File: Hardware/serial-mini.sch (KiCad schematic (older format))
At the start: 70 parts, among them J1 PICKIT V3 Header, J2 USB Micro B, J3 Serial Port, Q1 IRLML2060, Q2 IRLML2060, Q3 IRLML2060, U1 SIT2001BI-S2-33S-100.000000D, U2 FT230XQ-R, U3 DSPIC33CK64MP102, U4 SN74AHC14RGYR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

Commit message: Continue routing
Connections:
- net Status: now reaches U3.RB12
- net Status: now also D5.1, TP6.1
- removed net 2V@15mA: D5.1, TP6.1, U3.RA1
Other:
- moved on the sheet: D5, R17, TP6
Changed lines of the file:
@@
 	12600 6800 12600 6500
 Connection ~ 12600 6800
-NoConn ~ 9000 4750
 NoConn ~ 3100 4300
 NoConn ~ 3100 4000
@@
 L power:+5V #PWR015
 U 1 1 5F297A7B
-P 4550 3750
-F 0 "#PWR015" H 4550 3600 50  0001 C CNN
-F 1 "+5V" H 4565 3923 50  0000 C CNN
-F 2 "" H 4550 3750 50  0001 C CNN
-F 3 "" H 4550 3750 50  0001 C CNN
-	1    4550 3750
+P 4050 3700
+F 0 "#PWR015" H 4050 3550 50  0001 C CNN
+F 1 "+5V" H 4065 3873 50  0000 C CNN
+F 2 "" H 4050 3700 50  0001 C CNN
+F 3 "" H 4050 3700 50  0001 C CNN
+	1    4050 3700
 	0    -1   -1   0
 $EndComp
@@
 L serial-mini:VAOL-S8WR4 D5
 U 1 1 5F2EDA7B
-P 5400 3750
-F 0 "D5" H 5600 4138 60  0000 C CNN
-F 1 "VAOL-S8WR4" H 5600 4032 60  0000 C CNN
-F 2 "footprints:VAOL-S8WR4" H 5600 3390 60  0001 C CNN
-F 3 "http://vcclite.com/_pdf/VAOL-S8WR4-LED-0805-white.pdf" H 5600 4032 60  0001 C CNN
-	1    5400 3750
+P 4900 3700
+F 0 "D5" H 5100 4088 60  0000 C CNN
+F 1 "VAOL-S8WR4" H 5100 3982 60  0000 C CNN
+F 2 "footprints:VAOL-S8WR4" H 5100 3340 60  0001 C CNN
+F 3 "http://vcclite.com/_pdf/VAOL-S8WR4-LED-0805-white.pdf" H 5100 3982 60  0001 C CNN
+	1    4900 3700
 	1    0    0    -1
 $EndComp
@@
 $EndComp
 Wire Wire Line
-	5800 3750 5850 3750
+	5300 3700 5350 3700
 $Comp
 L serial-mini-rescue:RESISTOR0603-serial-mini-serial-mini R17
 U 1 1 5F3D4344
-P 5050 3750
-F 0 "R17" H 5050 4050 45  0000 C CNN
-F 1 "133" H 5050 3966 45  0000 C CNN
-F 2 "Resistor_SMD:R_0603_1608Metric_Pad1.05x0.95mm_HandSolder" H 5050 3900 20  0001 C CNN
-F 3 "" H 5050 3750 60  0001 C CNN
-F 4 " " H 5050 3871 60  0000 C CNN "Field4"
-	1    5050 3750
-	1    0    0    -1
-$EndComp
-Wire Wire Line
-	5250 3750 5400 3750
-Wire Wire Line
-	4850 3750 4550 3750
+P 4550 3700
+F 0 "R17" H 4550 4000 45  0000 C CNN
+F 1 "133" H 4550 3916 45  0000 C CNN
+F 2 "Resistor_SMD:R_0603_1608Metric_Pad1.05x0.95mm_HandSolder" H 4550 3850 20  0001 C CNN
+F 3 "" H 4550 3700 60  0001 C CNN
+F 4 " " H 4550 3821 60  0000 C CNN "Field4"
+	1    4550 3700
+	1    0    0    -1
+$EndComp
+Wire Wire Line
+	4750 3700 4900 3700
+Wire Wire Line
+	4350 3700 4050 3700
 Wire Wire Line
 	10050 6500 10100 6500
@@
 Text Label 10800 6500 0    50   ~ 0
 3V@20mA
-Text Label 5850 3750 0    50   ~ 0
+Text Label 5350 3700 0    50   ~ 0
 2V@15mA
 $Comp
@@
 L Connector:TestPoint TP6
 U 1 1 5F68536D
-P 5850 3750
-F 0 "TP6" H 5792 3776 50  0000 R CNN
-F 1 "TestPoint" H 5792 3867 50  0000 R CNN
-F 2 "TestPoint:TestPoint_Pad_1.0x1.0mm" H 6050 3750 50  0001 C CNN
-F 3 "~" H 6050 3750 50  0001 C CNN
-	1    5850 3750
-	-1   0    0    1
-$EndComp
-Connection ~ 5850 3750
-Wire Wire Line
-	5850 3750 6200 3750
+P 5350 3700
+F 0 "TP6" H 5292 3726 50  0000 R CNN
+F 1 "TestPoint" H 5292 3817 50  0000 R CNN
+F 2 "TestPoint:TestPoint_Pad_1.0x1.0mm" H 5550 3700 50  0001 C CNN
+F 3 "~" H 5550 3700 50  0001 C CNN
+	1    5350 3700
+	-1   0    0    1
+$EndComp
 $Comp
 L Connector:TestPoint TP1
@@
 NoConn ~ 4050 4700
 NoConn ~ 7550 3200
+Text GLabel 9000 4750 2    50   Input ~ 0
+Status
+Text GLabel 5350 3700 2    50   Input ~ 0
+Status
+NoConn ~ 6200 3750
 $EndSCHEMATC

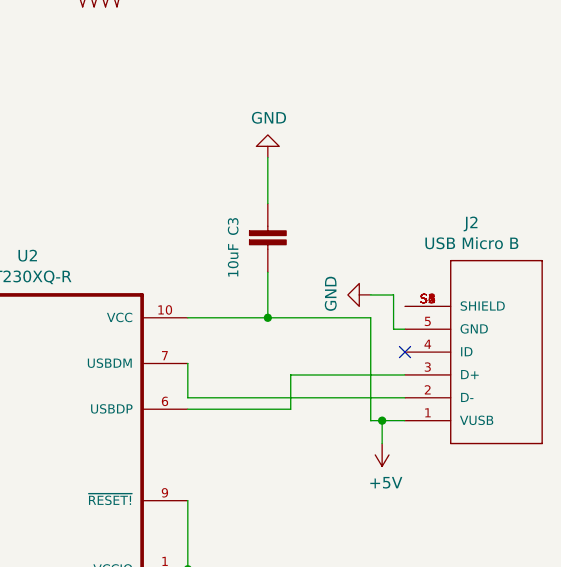
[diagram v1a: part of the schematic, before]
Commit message: Add missing courtyards
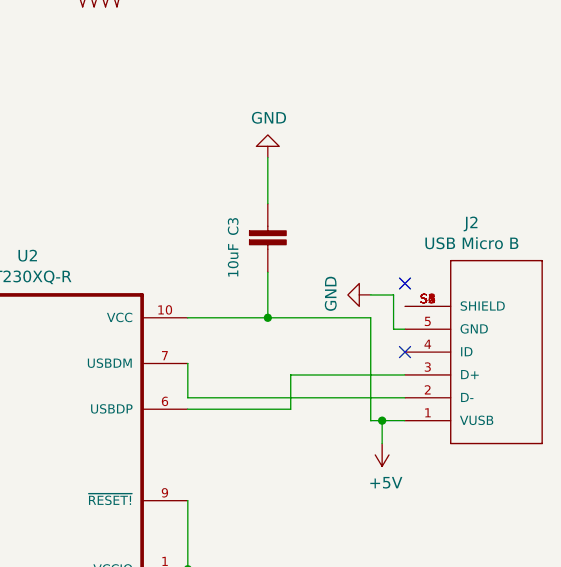
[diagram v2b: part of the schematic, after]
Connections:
- no-connect marks 30 -> 31
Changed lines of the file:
@@
 Status
 NoConn ~ 6200 3750
+NoConn ~ 13550 5550
 $EndSCHEMATC

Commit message: Add EMI/ESD protection on USB port
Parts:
- added C13, C9: 47pF, Capacitor_SMD:C_0603_1608Metric_Pad1.05x0.95mm_HandSolder, symbol serial-mini:Capacitor
- added C14: 4.7nF, Capacitor_SMD:C_0603_1608Metric_Pad1.05x0.95mm_HandSolder, symbol serial-mini:Capacitor
- added C15: 10nF, Capacitor_SMD:C_0603_1608Metric_Pad1.05x0.95mm_HandSolder, symbol serial-mini:Capacitor
- added D6: PRTR5V0U2F,115, footprints:Nexperia-SOT886-11_2018-0-MFG, symbol serial-mini:PRTR5V0U2F,115
- added FB1: Ferrite_Bead_Small, symbol Device:Ferrite_Bead_Small
- added R21, R22: 27, Resistor_SMD:R_0603_1608Metric_Pad1.05x0.95mm_HandSolder, symbol serial-mini-rescue:RESISTOR0603-serial-mini-serial-mini
- added R23: 1M, Resistor_SMD:R_0603_1608Metric_Pad1.05x0.95mm_HandSolder, symbol serial-mini:Resistor
- added U?: MAX232, symbol Interface_UART:MAX232
- J2: footprint footprints:FCI_10118193-0001LF -> footprints:AMPHENOL_10103593-0001LF
- TP11, TP12, TP13, TP14, TP15, TP16, TP17, TP18: footprint (none) -> TestPoint:TestPoint_THTPad_1.0x1.0mm_Drill0.5mm
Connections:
- net +5V: now also FB1.2; no longer J2.1 (VUSB)
- net GND: now also C13.2, C14.1, C15.1, C9.1, R23.2
- net PWM-Hue: now also U3.RB2; no longer U3.RB10
- net TX: now also U3.RB11; no longer U3.RB2
- net at J2.2 (D-): now also D6.3 (I/O2); no longer U2.7 (USBDM)
- net at J2.3 (D+): now also D6.1 (I/O1); no longer U2.6 (USBDP)
- net at J2.S1 (SHIELD), J2.S2 (SHIELD), J2.S3 (SHIELD)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: now also C14.2, D6.2 (GND), R23.1
- new net: R22.1, U2.6 (USBDP)
- new net: R21.1, U2.7 (USBDM)
- new net: C9.2, D6.4 (I/O2), R21.2
- new net: C13.1, D6.6 (I/O1), R22.2
- new net VBUS: C15.2, D6.5 (VCC), FB1.1, J2.1 (VUSB)
- no-connect marks 31 -> 29
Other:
- moved on the sheet: C1, C10, C11, C12, C2, C3, C4, C5, C6, C7, C8, D1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

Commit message: Use hierarchical sheets
Added MAX232 also
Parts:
- removed C1, C4, C7, C8: 0.1UF, Capacitor_SMD:C_0603_1608Metric_Pad1.05x0.95mm_HandSolder, symbol serial-mini:Capacitor
- removed C11: 0.1uF, Capacitor_SMD:C_0603_1608Metric_Pad1.05x0.95mm_HandSolder, symbol serial-mini:Capacitor
- removed C12, C2: 1UF, Capacitor_SMD:C_0603_1608Metric_Pad1.05x0.95mm_HandSolder, symbol serial-mini:Capacitor
- removed C13, C9: 47pF, Capacitor_SMD:C_0603_1608Metric_Pad1.05x0.95mm_HandSolder, symbol serial-mini:Capacitor
- removed C14: 4.7nF, Capacitor_SMD:C_0603_1608Metric_Pad1.05x0.95mm_HandSolder, symbol serial-mini:Capacitor
- removed C15: 10nF, Capacitor_SMD:C_0603_1608Metric_Pad1.05x0.95mm_HandSolder, symbol serial-mini:Capacitor
- removed C3: 10uF, Capacitor_SMD:C_0603_1608Metric_Pad1.05x0.95mm_HandSolder, symbol serial-mini:Capacitor
- removed D1: LTST-C171KSKT, footprints:DIOC200X125X110, symbol serial-mini:LTST-C171KSKT
- removed D2, D3, D4: LED, footprints:CLVBA-FKA-CAEDH8BBB7A363, symbol serial-mini:SMD-LED-RGB(4P-0606)
- removed D6: PRTR5V0U2F,115, footprints:Nexperia-SOT886-11_2018-0-MFG, symbol serial-mini:PRTR5V0U2F,115
- removed FB1: Ferrite_Bead_Small, symbol Device:Ferrite_Bead_Small
- removed J2: USB Micro B, footprints:AMPHENOL_10103593-0001LF, symbol serial-mini:10118193-0001LF
- removed J3: Serial Port, footprints:3-106505-2, symbol serial-mini:3-106505-2
- removed Q1, Q2, Q3: IRLML2060, footprints:IRLML2060TRPBF, symbol Device:Q_NMOS_GDS
- removed R1, R2, R3, R4, R5, R6: 10k, Resistor_SMD:R_0603_1608Metric_Pad1.05x0.95mm_HandSolder, symbol serial-mini:Resistor
- removed R10, R12, R14: 130, Resistor_SMD:R_0603_1608Metric_Pad1.05x0.95mm_HandSolder, symbol serial-mini:Resistor
- removed R11, R7, R9: 74, Resistor_SMD:R_0603_1608Metric_Pad1.05x0.95mm_HandSolder, symbol serial-mini:Resistor
- removed R13, R15, R16: 90, Resistor_SMD:R_0603_1608Metric_Pad1.05x0.95mm_HandSolder, symbol serial-mini:Resistor
- removed R18, R19: 3352T-1-103LF, footprints:TRIM_3352T-1-103LF, symbol serial-mini:3352T-1-103LF
- removed R20: 150, Resistor_SMD:R_0603_1608Metric_Pad1.05x0.95mm_HandSolder, symbol serial-mini-rescue:RESISTOR0603-serial-mini-serial-mini
- removed R21, R22: 27, Resistor_SMD:R_0603_1608Metric_Pad1.05x0.95mm_HandSolder, symbol serial-mini-rescue:RESISTOR0603-serial-mini-serial-mini
- removed R23: 1M, Resistor_SMD:R_0603_1608Metric_Pad1.05x0.95mm_HandSolder, symbol serial-mini:Resistor
- removed S1, S2, S3: KAILH_HOT_SWAP, footprints:Kailh_MX_Socket, symbol serial-mini:KAILH_HOT_SWAP
- removed TP-3.3V1, TP-5V1, TP-GND1, TP1, TP2, TP3, TP4: TestPoint, TestPoint:TestPoint_Pad_1.0x1.0mm, symbol Connector:TestPoint
- removed TP11, TP12, TP13, TP14, TP15, TP16, TP17, TP18: TestPoint, TestPoint:TestPoint_THTPad_1.0x1.0mm_Drill0.5mm, symbol Connector:TestPoint
- removed U1: SIT2001BI-S2-33S-100.000000D, footprints:SIT2001BI-S2-33S-100.000000D, symbol serial-mini:SIT2001BI-S2-33S-100.000000D
- removed U2: FT230XQ-R, footprints:FT230XQ, symbol serial-mini:FT230XQ-R
- removed U4: SN74AHC14RGYR, footprints:SN74AHC14RGYR, symbol serial-mini:SN74AHC14RGYR
- removed U5: MIC5504-3.3YM5-TR, footprints:MIC5504, symbol serial-mini:MIC5504-3.3YM5-TR
- removed U?: MAX232, symbol Interface_UART:MAX232
- R17: symbol serial-mini-rescue:RESISTOR0603-serial-mini-serial-mini -> serial-mini:Resistor
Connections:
- net 100MHz Oscillator/OSCO: now reaches U3.RB0
- net USB to UART/RX-USB: now reaches U3.RB6
- net USB to UART/TX-USB: now reaches U3.RB7
- net Blue renamed Backlight/Blue
- net Green renamed Backlight/Green
- net PWM-Brightness renamed Brightness
- net PWM-Hue renamed Backlight/Hue
- net RX renamed TTL to RS232 Converter/RX-Serial-Port
- net Red renamed Backlight/Red
- net SWITCH_OUT_1 renamed Debounce/Switch_Out_1
- net SWITCH_OUT_2 renamed Debounce/Switch_Out_2
- net SWITCH_OUT_3 renamed Debounce/Switch_Out_3
- net TX renamed TX-Serial-Port
- no-connect marks 29 -> 7
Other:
- moved on the sheet: C10, C5, C6, D5, H1, H2, H3, H4, J1, R17, R8, TP6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

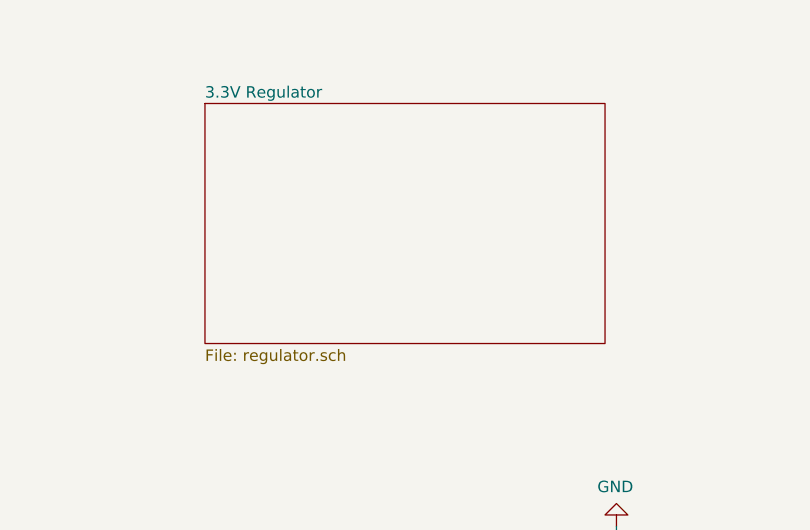
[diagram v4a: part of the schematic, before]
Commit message: Complete new schematic
Added MAX232 and fixed test points on switches
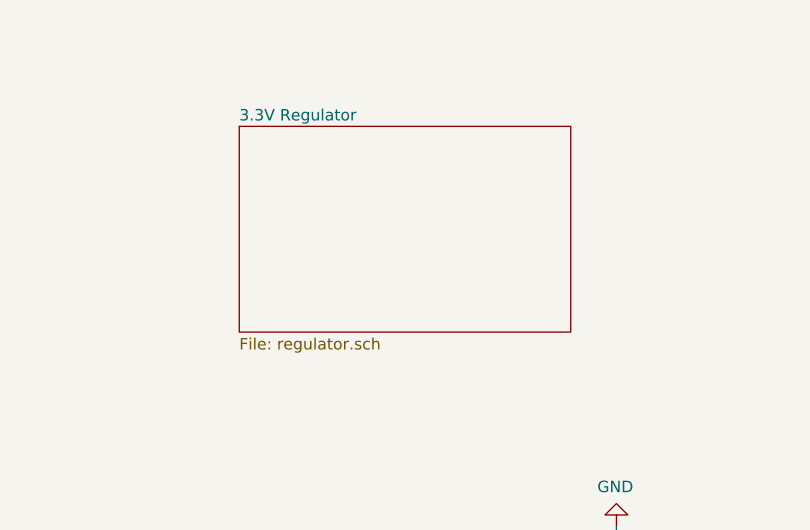
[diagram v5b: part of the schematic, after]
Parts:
- TP6: footprint TestPoint:TestPoint_Pad_1.0x1.0mm -> TestPoint:TestPoint_THTPad_1.0x1.0mm_Drill0.5mm
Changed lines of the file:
@@
 F 0 "TP6" H 6192 4826 50  0000 R CNN
 F 1 "TestPoint" H 6192 4917 50  0000 R CNN
-F 2 "TestPoint:TestPoint_Pad_1.0x1.0mm" H 6450 4800 50  0001 C CNN
+F 2 "TestPoint:TestPoint_THTPad_1.0x1.0mm_Drill0.5mm" H 6450 4800 50  0001 C CNN
 F 3 "~" H 6450 4800 50  0001 C CNN
 	1    6250 4800
@@
 	10450 5650 9900 5650
 $Sheet
-S 7450 2550 1750 1050
+S 7600 2650 1450 900
 U 5F6537ED
 F0 "3.3V Regulator" 50

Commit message: Add more net labels
Begin redesigning PCB again
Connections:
- net MCLR: now reaches J1.MCLR, R8.1, U3.MCLR
- net 100MHz Oscillator/OSCO renamed OSCO
- net Backlight/Blue renamed Green
- net Backlight/Green renamed Blue
- net Backlight/Hue renamed Hue
- net Backlight/Red renamed Red
- net Debounce/Switch_Out_1 renamed S1
- net Debounce/Switch_Out_2 renamed S2
- net Debounce/Switch_Out_3 renamed S3
- net TTL to RS232 Converter/RX-Serial-Port renamed RX-Serial-Port
- net USB to UART/RX-USB renamed UART-RX
- net USB to UART/TX-USB renamed UART-TX
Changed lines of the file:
@@
 	10450 5650 9900 5650
-$Sheet
-S 7600 2650 1450 900
-U 5F6537ED
-F0 "3.3V Regulator" 50
-F1 "regulator.sch" 50
-$EndSheet
 $Sheet
 S 4400 5750 600  600
@@
 F0 "USB to UART" 50
 F1 "usb-uart.sch" 50
-F2 "RX-USB" I L 11250 7450 50
-F3 "TX-USB" I L 11250 7250 50
+F2 "USB-RX" I L 11250 7450 50
+F3 "USB-TX" I L 11250 7250 50
 $EndSheet
 Wire Wire Line
@@
 F0 "TTL to RS232 Converter" 50
 F1 "rs232-converter.sch" 50
-F2 "RX-Serial-Port" I R 5250 6850 50
-F3 "TX-Serial-Port" I R 5250 7000 50
+F2 "Serial-Port-RX" I R 5250 6850 50
+F3 "Serial-Port-TX" I R 5250 7000 50
 $EndSheet
 Text Label 9900 4850 0    50   ~ 0
@@
 Status
 Text Label 5250 7000 0    50   ~ 0
-TX-Serial-Port
+Serial-Port-TX
 Text Label 11150 4350 3    50   ~ 0
 PGD
@@
 Text Label 6250 4800 0    50   ~ 0
 Status
+$Sheet
+S 7500 2400 1850 1200
+U 5F22B342
+F0 "3.3V Regulator" 50
+F1 "power-regulator.sch" 50
+$EndSheet
+Text Label 10150 5250 0    50   ~ 0
+S2
+Text Label 10150 5450 0    50   ~ 0
+S3
+Text Label 10150 5650 0    50   ~ 0
+S1
+Text Label 10150 5050 0    50   ~ 0
+MCLR
+Text Label 10150 7450 0    50   ~ 0
+UART-RX
+Text Label 6850 6850 0    50   ~ 0
+Hue
+Text Label 6850 7050 0    50   ~ 0
+Red
+Text Label 6850 7250 0    50   ~ 0
+Green
+Text Label 6850 7450 0    50   ~ 0
+Blue
+Text Label 6100 6650 0    50   ~ 0
+RX-Serial-Port
+Text Label 5500 6250 0    50   ~ 0
+OSCO
+Text Label 10150 7250 0    50   ~ 0
+UART-TX
 $EndSCHEMATC
